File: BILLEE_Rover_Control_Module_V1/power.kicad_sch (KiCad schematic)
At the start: 79 parts, among them CN1 XT90PW-M.G.Y, U10 +22.2V_POE_POWER, U2 TPS1HA08BQPWPRQ1, U20 +12V_NET_SW_PWR, U23 TPS1HA08BQPWPRQ1, U24 LT8612EUDE#TRPBF, U25 +12V_AUX_PWR, U38 MCP9808T-E/MS, U5 TPS1HA08BQPWPRQ1, U6 INA780BIDEKR, U7 LT8612EUDE#TRPBF, U8 LT8612EUDE#TRPBF, U9 +20V_JETSON_PWR

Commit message: More goodies.
Did a review with claude and patched a lot of missng things. Updated RCP for LOGIC and more.
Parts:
- added D10, D11, D12: BAS21, Package_TO_SOT_SMD:SOT-23, symbol Diode:BAS21
- added R100, R101, R99: 4.7k, symbol Device:R_US
- C19, C20, C26, C27, C40, C41: Voltage (none) -> 50V
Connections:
- net GND: now also D10.3 (K), D11.3 (K), D12.3 (K), R100.1, R101.1, R99.1; no longer U2.1 (GND), U23.1 (GND), U5.1 (GND)
- new net: D10.1 (A), R99.2, U2.1 (GND)
- new net: D11.1 (A), R100.2, U5.1 (GND)
- new net: D12.1 (A), R101.2, U23.1 (GND)

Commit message: Biggus Goodies
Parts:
- R100, R101, R26, R27, R28, R29, R30, R31, R32, R33, R34, R35, R36, R37, R38, R39, R40, R41, R42, R43, R44, R45, R46, R47, R59, R61, R62, R63, R64, R65, R66, R67, R68, R69, R72, R99: footprint (none) -> Resistor_SMD:R_0402_1005Metric
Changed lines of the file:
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@@
 			)
 		)
-		(property "Footprint" ""
+		(property "Footprint" "Resistor_SMD:R_0402_1005Metric"
 			(at 240.284 202.946 90)
 			(hide yes)
@@
 			)
 		)
-		(property "Footprint" ""
+		(property "Footprint" "Resistor_SMD:R_0402_1005Metric"
 			(at 203.454 119.634 90)
 			(hide yes)
@@
 			)
 		)
-		(property "Footprint" ""
+		(property "Footprint" "Resistor_SMD:R_0402_1005Metric"
 			(at 264.414 78.486 90)
 			(hide yes)
@@
 			)
 		)
-		(property "Footprint" ""
+		(property "Footprint" "Resistor_SMD:R_0402_1005Metric"
 			(at 145.796 49.784 90)
 			(hide yes)
@@
 			)
 		)
-		(property "Footprint" ""
+		(property "Footprint" "Resistor_SMD:R_0402_1005Metric"
 			(at 294.386 146.304 90)
 			(hide yes)
@@
 			)
 		)
-		(property "Footprint" ""
+		(property "Footprint" "Resistor_SMD:R_0402_1005Metric"
 			(at 296.926 139.446 90)
 			(hide yes)
@@
 			)
 		)
-		(property "Footprint" ""
+		(property "Footprint" "Resistor_SMD:R_0402_1005Metric"
 			(at 194.564 139.446 90)
 			(hide yes)
@@
 			)
 		)
-		(property "Footprint" ""
+		(property "Footprint" "Resistor_SMD:R_0402_1005Metric"
 			(at 162.306 54.864 90)
 			(hide yes)
@@
 			)
 		)
-		(property "Footprint" ""
+		(property "Footprint" "Resistor_SMD:R_0402_1005Metric"
 			(at 143.256 125.984 90)
 			(hide yes)
@@
 			)
 		)
-		(property "Footprint" ""
+		(property "Footprint" "Resistor_SMD:R_0402_1005Metric"
 			(at 261.874 154.686 90)
 			(hide yes)
@@
 			)
 		)
-		(property "Footprint" ""
+		(property "Footprint" "Resistor_SMD:R_0402_1005Metric"
 			(at 299.466 63.246 90)
 			(hide yes)
@@
 			)
 		)
-		(property "Footprint" ""
+		(property "Footprint" "Resistor_SMD:R_0402_1005Metric"
 			(at 296.926 70.104 90)
 			(hide yes)
@@
 			)
 		)
-		(property "Footprint" ""
+		(property "Footprint" "Resistor_SMD:R_0402_1005Metric"
 			(at 143.256 118.364 90)
 			(hide yes)
@@
 			)
 		)
-		(property "Footprint" ""
+		(property "Footprint" "Resistor_SMD:R_0402_1005Metric"
 			(at 236.474 129.286 90)
 			(hide yes)
@@
 			)
 		)
-		(property "Footprint" ""
+		(property "Footprint" "Resistor_SMD:R_0402_1005Metric"
 			(at 239.014 53.086 90)
 			(hide yes)
@@
 			)
 		)
-		(property "Footprint" ""
+		(property "Footprint" "Resistor_SMD:R_0402_1005Metric"
 			(at 154.686 54.864 90)
 			(hide yes)
@@
 			)
 		)
-		(property "Footprint" ""
+		(property "Footprint" "Resistor_SMD:R_0402_1005Metric"
 			(at 239.014 42.926 90)
 			(hide yes)
@@
 			)
 		)
-		(property "Footprint" ""
+		(property "Footprint" "Resistor_SMD:R_0402_1005Metric"
 			(at 198.374 213.106 90)
 			(hide yes)
@@
 			)
 		)
-		(property "Footprint" ""
+		(property "Footprint" "Resistor_SMD:R_0402_1005Metric"
 			(at 148.336 192.024 90)
 			(hide yes)
@@
 			)
 		)
-		(property "Footprint" ""
+		(property "Footprint" "Resistor_SMD:R_0402_1005Metric"
 			(at 205.994 43.434 90)
 			(hide yes)
@@
 			)
 		)
-		(property "Footprint" ""
+		(property "Footprint" "Resistor_SMD:R_0402_1005Metric"
 			(at 148.336 199.644 90)
 			(hide yes)
@@
 			)
 		)
-		(property "Footprint" ""
+		(property "Footprint" "Resistor_SMD:R_0402_1005Metric"
 			(at 155.956 204.724 90)
 			(hide yes)
@@
 			)
 		)
-		(property "Footprint" ""
+		(property "Footprint" "Resistor_SMD:R_0402_1005Metric"
 			(at 207.264 195.834 90)
 			(hide yes)
@@
 			)
 		)
-		(property "Footprint" ""
+		(property "Footprint" "Resistor_SMD:R_0402_1005Metric"
 			(at 203.454 122.174 90)
 			(hide yes)
@@
 			)
 		)
-		(property "Footprint" ""
+		(property "Footprint" "Resistor_SMD:R_0402_1005Metric"
 			(at 159.766 131.064 90)
 			(hide yes)
@@
 			)
 		)
-		(property "Footprint" ""
+		(property "Footprint" "Resistor_SMD:R_0402_1005Metric"
 			(at 300.736 213.106 90)
 			(hide yes)
@@
 			)
 		)
-		(property "Footprint" ""
+		(property "Footprint" "Resistor_SMD:R_0402_1005Metric"
 			(at 236.474 119.126 90)
 			(hide yes)
@@
 			)
 		)
-		(property "Footprint" ""
+		(property "Footprint" "Resistor_SMD:R_0402_1005Metric"
 			(at 265.684 228.346 90)
 			(hide yes)
@@
 			)
 		)
-		(property "Footprint" ""
+		(property "Footprint" "Resistor_SMD:R_0402_1005Metric"
 			(at 298.196 219.964 90)
 			(hide yes)
@@
 			)
 		)
-		(property "Footprint" ""
+		(property "Footprint" "Resistor_SMD:R_0402_1005Metric"
 			(at 240.284 192.786 90)
 			(hide yes)
@@
 			)
 		)
-		(property "Footprint" ""
+		(property "Footprint" "Resistor_SMD:R_0402_1005Metric"
 			(at 197.104 63.246 90)
 			(hide yes)
@@
 			)
 		)
-		(property "Footprint" ""
+		(property "Footprint" "Resistor_SMD:R_0402_1005Metric"
 			(at 205.994 45.974 90)
 			(hide yes)
@@
 			)
 		)
-		(property "Footprint" ""
+		(property "Footprint" "Resistor_SMD:R_0402_1005Metric"
 			(at 145.796 42.164 90)
 			(hide yes)
@@
 			)
 		)
-		(property "Footprint" ""
+		(property "Footprint" "Resistor_SMD:R_0402_1005Metric"
 			(at 207.264 193.294 90)
 			(hide yes)
@@
 			)
 		)
-		(property "Footprint" ""
+		(property "Footprint" "Resistor_SMD:R_0402_1005Metric"
 			(at 163.576 204.724 90)
 			(hide yes)
@@
 			)
 		)
-		(property "Footprint" ""
+		(property "Footprint" "Resistor_SMD:R_0402_1005Metric"
 			(at 152.146 131.064 90)
 			(hide yes)

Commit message: Fixes
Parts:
- removed U10: +22.2V_POE_POWER, PDB_LCSC:CONN-TH_P5.00_KF301-5.0-2P, symbol PDB_LCSC_Libs:KF301-5.0-2P
- removed U20: +12V_NET_SW_PWR, PDB_LCSC:CONN-TH_P5.00_KF301-5.0-2P, symbol PDB_LCSC_Libs:KF301-5.0-2P
- removed U25: +12V_AUX_PWR, PDB_LCSC:CONN-TH_P5.00_KF301-5.0-2P, symbol PDB_LCSC_Libs:KF301-5.0-2P
- removed U9: +20V_JETSON_PWR, PDB_LCSC:CONN-TH_P5.00_KF301-5.0-2P, symbol PDB_LCSC_Libs:KF301-5.0-2P
- added CN15, CN16, CN17, CN18: XT60PW-M, PDB_LCSC:CONN-TH_XT60PW-M, symbol PDB_LCSC_Libs:XT60PW-M
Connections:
- net +12V_AUX_VCC: now also CN17.2 (+), CN18.2 (+)
- net +20V_JETSON_VCC: now also CN15.2 (+)
- net +22.2V_POE_VCC: now also CN16.2 (+)
- net GND: now also CN15.1 (-), CN15.3, CN15.4, CN16.1 (-), CN16.3, CN16.4, CN17.1 (-), CN17.3, CN17.4, CN18.1 (-)
- new net: CN18.3, CN18.4

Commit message: Schematic Fixed in NO RCP yet
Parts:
- C1: footprint (none) -> Capacitor_SMD:C_0402_1005Metric
- C15, C16, C17, C18, C21, C22, C23, C24, C25, C35, C36, C37, C38, C39, C62, C63, C64: footprint (none) -> Capacitor_SMD:C_0603_1608Metric
- C19, C20, C26, C27, C40, C41: footprint (none) -> Capacitor_SMD:C_1210_3225Metric
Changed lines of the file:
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@@
 			)
 		)
-		(property "Footprint" ""
+		(property "Footprint" "Capacitor_SMD:C_1210_3225Metric"
 			(at 313.3852 125.73 0)
 			(hide yes)
@@
 			)
 		)
-		(property "Footprint" ""
+		(property "Footprint" "Capacitor_SMD:C_0603_1608Metric"
 			(at 297.18 185.7248 0)
 			(hide yes)
@@
 			)
 		)
-		(property "Footprint" ""
+		(property "Footprint" "Capacitor_SMD:C_0603_1608Metric"
 			(at 253.6952 223.52 0)
 			(hide yes)
@@
 			)
 		)
-		(property "Footprint" ""
+		(property "Footprint" "Capacitor_SMD:C_0603_1608Metric"
 			(at 295.91 67.0052 0)
 			(hide yes)
@@
 			)
 		)
-		(property "Footprint" ""
+		(property "Footprint" "Capacitor_SMD:C_0603_1608Metric"
 			(at 293.37 143.2052 0)
 			(hide yes)
@@
 			)
 		)
-		(property "Footprint" ""
+		(property "Footprint" "Capacitor_SMD:C_0603_1608Metric"
 			(at 135.5852 201.93 0)
 			(hide yes)
@@
 			)
 		)
-		(property "Footprint" ""
+		(property "Footprint" "Capacitor_SMD:C_0603_1608Metric"
 			(at 297.18 216.8652 0)
 			(hide yes)
@@
 			)
 		)
-		(property "Footprint" ""
+		(property "Footprint" "Capacitor_SMD:C_0603_1608Metric"
 			(at 221.9452 196.85 0)
 			(hide yes)
@@
 			)
 		)
-		(property "Footprint" ""
+		(property "Footprint" "Capacitor_SMD:C_0603_1608Metric"
 			(at 220.6752 46.99 0)
 			(hide yes)
@@
 			)
 		)
-		(property "Footprint" ""
+		(property "Footprint" "Capacitor_SMD:C_0603_1608Metric"
 			(at 238.4552 147.32 0)
 			(hide yes)
@@
 			)
 		)
-		(property "Footprint" ""
+		(property "Footprint" "Capacitor_SMD:C_1210_3225Metric"
 			(at 328.6252 199.39 0)
 			(hide yes)
@@
 			)
 		)
-		(property "Footprint" ""
+		(property "Footprint" "Capacitor_SMD:C_0603_1608Metric"
 			(at 249.8852 149.86 0)
 			(hide yes)
@@
 			)
 		)
-		(property "Footprint" ""
+		(property "Footprint" "Capacitor_SMD:C_1210_3225Metric"
 			(at 315.9252 49.53 0)
 			(hide yes)
@@
 			)
 		)
-		(property "Footprint" ""
+		(property "Footprint" "Capacitor_SMD:C_0603_1608Metric"
 			(at 295.91 35.8648 0)
 			(hide yes)
@@
 			)
 		)
-		(property "Footprint" ""
+		(property "Footprint" "Capacitor_SMD:C_1210_3225Metric"
 			(at 327.3552 49.53 0)
 			(hide yes)
@@
 			)
 		)
-		(property "Footprint" ""
+		(property "Footprint" "Capacitor_SMD:C_0402_1005Metric"
 			(at 134.3152 52.07 0)
 			(hide yes)
@@
 			)
 		)
-		(property "Footprint" ""
+		(property "Footprint" "Capacitor_SMD:C_0603_1608Metric"
 			(at 242.2652 220.98 0)
 			(hide yes)
@@
 			)
 		)
-		(property "Footprint" ""
+		(property "Footprint" "Capacitor_SMD:C_0603_1608Metric"
 			(at 293.37 112.0648 0)
 			(hide yes)
@@
 			)
 		)
-		(property "Footprint" ""
+		(property "Footprint" "Capacitor_SMD:C_0603_1608Metric"
 			(at 252.4252 73.66 0)
 			(hide yes)
@@
 			)
 		)
-		(property "Footprint" ""
+		(property "Footprint" "Capacitor_SMD:C_0603_1608Metric"
 			(at 218.1352 123.19 0)
 			(hide yes)
@@
 			)
 		)
-		(property "Footprint" ""
+		(property "Footprint" "Capacitor_SMD:C_0603_1608Metric"
 			(at 131.7752 128.27 0)
 			(hide yes)
@@
 			)
 		)
-		(property "Footprint" ""
+		(property "Footprint" "Capacitor_SMD:C_1210_3225Metric"
 			(at 317.1952 199.39 0)
 			(hide yes)
@@
 			)
 		)
-		(property "Footprint" ""
+		(property "Footprint" "Capacitor_SMD:C_1210_3225Metric"
 			(at 324.8152 125.73 0)
 			(hide yes)
@@
 			)
 		)
-		(property "Footprint" ""
+		(property "Footprint" "Capacitor_SMD:C_0603_1608Metric"
 			(at 240.9952 71.12 0)
 			(hide yes)

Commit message: Updated footprint selection
Still missing the four inductors for the regulators, two of them can be poached from scales
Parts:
- C1: footprint Capacitor_SMD:C_0402_1005Metric -> Capacitor_SMD:C_0603_1608Metric
- C15, C16, C22, C23, C36, C37: footprint Capacitor_SMD:C_0603_1608Metric -> Capacitor_SMD:C_0402_1005Metric
- U2, U23, U5: footprint PDB_LCSC:HTSSOP-16_L5.0-W4.4-P0.65-LS6.4-BL-EP -> PDB_LCSC:HTSSOP-16_L5.0-W4.4-P0.65-LS6.4-TL-EP2.9
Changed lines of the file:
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@@
 			)
 		)
-		(property "Footprint" "Capacitor_SMD:C_0603_1608Metric"
+		(property "Footprint" "Capacitor_SMD:C_0402_1005Metric"
 			(at 253.6952 223.52 0)
 			(hide yes)
@@
 			)
 		)
-		(property "Footprint" "PDB_LCSC:HTSSOP-16_L5.0-W4.4-P0.65-LS6.4-BL-EP"
+		(property "Footprint" "PDB_LCSC:HTSSOP-16_L5.0-W4.4-P0.65-LS6.4-TL-EP2.9"
 			(at 184.15 64.77 0)
 			(hide yes)
@@
 			)
 		)
-		(property "Footprint" "PDB_LCSC:HTSSOP-16_L5.0-W4.4-P0.65-LS6.4-BL-EP"
+		(property "Footprint" "PDB_LCSC:HTSSOP-16_L5.0-W4.4-P0.65-LS6.4-TL-EP2.9"
 			(at 181.61 140.97 0)
 			(hide yes)
@@
 			)
 		)
-		(property "Footprint" "Capacitor_SMD:C_0603_1608Metric"
+		(property "Footprint" "Capacitor_SMD:C_0402_1005Metric"
 			(at 238.4552 147.32 0)
 			(hide yes)
@@
 			)
 		)
-		(property "Footprint" "PDB_LCSC:HTSSOP-16_L5.0-W4.4-P0.65-LS6.4-BL-EP"
+		(property "Footprint" "PDB_LCSC:HTSSOP-16_L5.0-W4.4-P0.65-LS6.4-TL-EP2.9"
 			(at 185.42 214.63 0)
 			(hide yes)
@@
 			)
 		)
-		(property "Footprint" "Capacitor_SMD:C_0603_1608Metric"
+		(property "Footprint" "Capacitor_SMD:C_0402_1005Metric"
 			(at 249.8852 149.86 0)
 			(hide yes)
@@
 			)
 		)
-		(property "Footprint" "Capacitor_SMD:C_0402_1005Metric"
+		(property "Footprint" "Capacitor_SMD:C_0603_1608Metric"
 			(at 134.3152 52.07 0)
 			(hide yes)
@@
 			)
 		)
-		(property "Footprint" "Capacitor_SMD:C_0603_1608Metric"
+		(property "Footprint" "Capacitor_SMD:C_0402_1005Metric"
 			(at 242.2652 220.98 0)
 			(hide yes)
@@
 			)
 		)
-		(property "Footprint" "Capacitor_SMD:C_0603_1608Metric"
+		(property "Footprint" "Capacitor_SMD:C_0402_1005Metric"
 			(at 252.4252 73.66 0)
 			(hide yes)
@@
 			)
 		)
-		(property "Footprint" "Capacitor_SMD:C_0603_1608Metric"
+		(property "Footprint" "Capacitor_SMD:C_0402_1005Metric"
 			(at 240.9952 71.12 0)
 			(hide yes)

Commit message: Updated footprints. I think schematic is officially finished.
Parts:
- removed L2: 1.8u, symbol Device:L
- removed L3: 35u, symbol Device:L
- removed L5: 10uh, symbol Device:L
- added L1: 1.8u, PDB_LCSC:L1210, symbol PDB_LCSC_Libs:NLV32T-1R8J-PF
- added SW1: 33uH, PDB_LCSC:IND-SMD_L13.5-W12.6, symbol PDB_LCSC_Libs:TMPA1265SP-330MN-D
- added U1: 10uH, PDB_LCSC:IND-SMD_L7.2-W6.6_GPSR07X0, symbol PDB_LCSC_Libs:CYA0630-10UH
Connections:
- net +12V_AUX_VCC: now also U1.2
- net +20V_JETSON_VCC: now also SW1.2
- net +3.3V_RP2350_VCC: now also L1.2
- net at C38.2, U24.15 (SW): now also U1.1
- net at C18.2, U7.15 (SW): now also L1.1
- net at C24.2, U8.15 (SW): now also SW1.1
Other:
- moved on the sheet: C39, R69

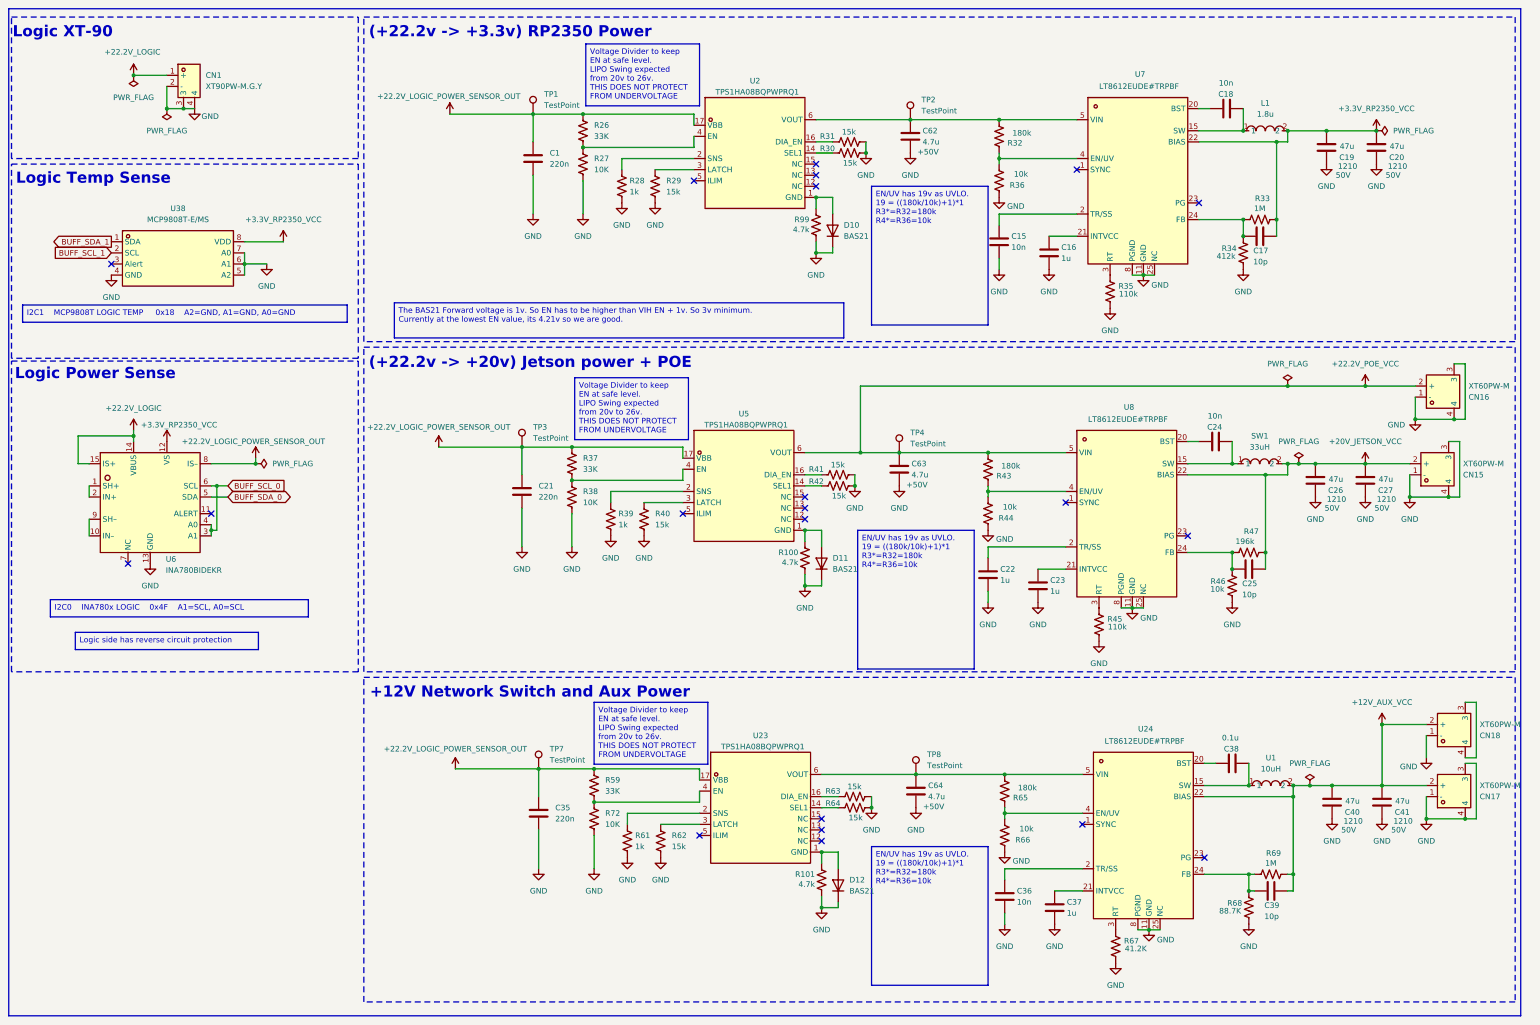
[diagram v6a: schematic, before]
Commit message: Updated reference designators. Schematic Complete
Not including RCP for Drivetrain/Arm/Science
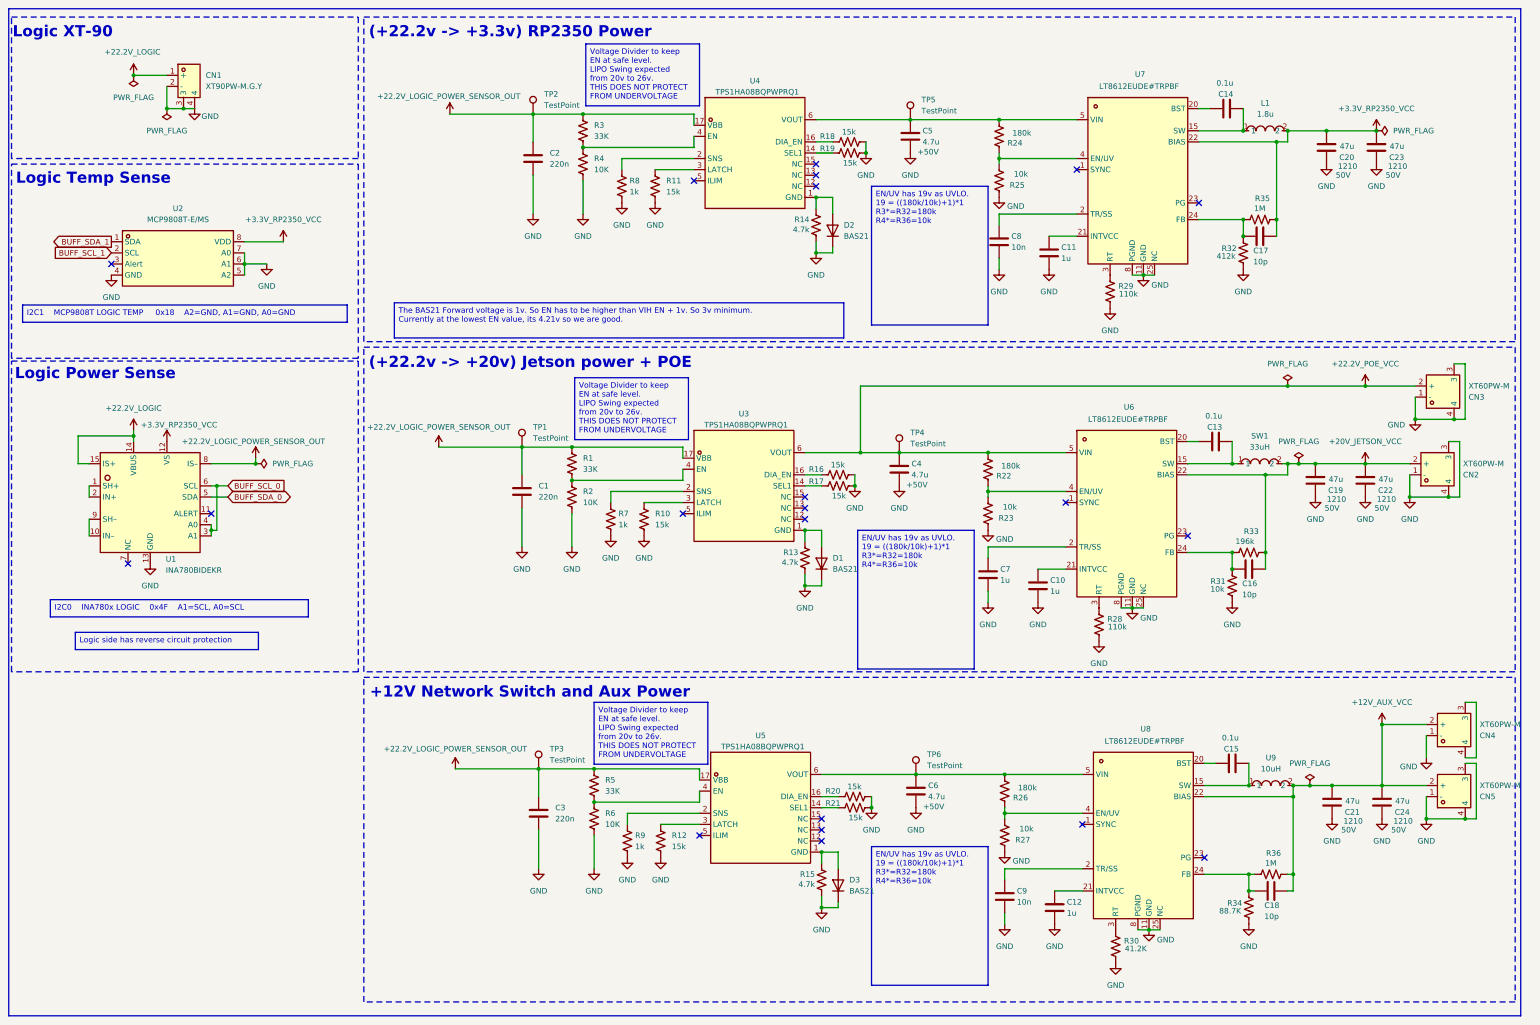
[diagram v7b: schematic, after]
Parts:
- C13: renamed from C24; value 10n -> 0.1u
- C14: renamed from C18; value 10n -> 0.1u
- renumbered C21 to C1, C23 to C10, C16 to C11, C37 to C12, C38 to C15, C25 to C16, C39 to C18, C26 to C19, C1 to C2, C19 to C20, C40 to C21, C27 to C22, C20 to C23, C41 to C24, C35 to C3, C63 to C4, C62 to C5, C64 to C6, C22 to C7, C15 to C8, C36 to C9, CN15 to CN2, CN16 to CN3, CN18 to CN4, CN17 to CN5, D11 to D1, D10 to D2, D12 to D3, R37 to R1, R40 to R10, R29 to R11, R62 to R12, R100 to R13, R99 to R14, R101 to R15, R41 to R16, R42 to R17, R31 to R18, R30 to R19, R38 to R2, R63 to R20, R64 to R21, R43 to R22, R44 to R23, R32 to R24, R36 to R25, R65 to R26, R66 to R27, R45 to R28, R35 to R29, R26 to R3, R67 to R30, R46 to R31, R34 to R32, R47 to R33, R68 to R34, R33 to R35, R69 to R36, R27 to R4, R59 to R5, R72 to R6, R39 to R7, R28 to R8, R61 to R9, TP3 to TP1, TP1 to TP2, TP7 to TP3, TP2 to TP5, TP8 to TP6, U6 to U1, U38 to U2, U5 to U3, U2 to U4, U23 to U5, U8 to U6, U24 to U8, U1 to U9

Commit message: Layout...
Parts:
- added C72: 0.1u, Capacitor_SMD:C_0603_1608Metric, symbol Device:C
- C20, C23: footprint Capacitor_SMD:C_1210_3225Metric -> Capacitor_SMD:C_01005_0402Metric; Package 1210 -> 0402; Voltage 50V -> 6V
- TP1, TP2, TP3, TP4, TP5, TP6: footprint Connector_Pin:Pin_D1.0mm_L10.0mm -> TestPoint:TestPoint_THTPad_2.0x2.0mm_Drill1.0mm
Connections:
- net +3.3V_RP2350_VCC: now also C72.2
- net GND: now also C72.1
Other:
- note added: "Load Switch"
- note added: "Switching Reg"
